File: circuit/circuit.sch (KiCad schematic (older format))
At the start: 9 parts

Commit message: Update schematic
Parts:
- gave numbers to parts that had none: 1
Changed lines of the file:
@@
 $EndDescr
-$Comp
-L Device:R_POT_US RV_THRESHOLD1
-U 1 1 61422150
-P 2950 1700
-F 0 "RV_THRESHOLD1" H 2882 1746 50  0000 R CNN
-F 1 "200K" H 2882 1655 50  0000 R CNN
-F 2 "" H 2950 1700 50  0001 C CNN
-F 3 "~" H 2950 1700 50  0001 C CNN
-	1    2950 1700
-	1    0    0    -1
-$EndComp
 $Comp
 L power:+5V #PWR0101
@@
 	1    0    0    -1
 $EndComp
-$Comp
-L power:Earth #PWR0102
-U 1 1 6142409F
-P 2950 1950
-F 0 "#PWR0102" H 2950 1700 50  0001 C CNN
-F 1 "Earth" H 2950 1800 50  0001 C CNN
-F 2 "" H 2950 1950 50  0001 C CNN
-F 3 "~" H 2950 1950 50  0001 C CNN
-	1    2950 1950
-	1    0    0    -1
-$EndComp
-Wire Wire Line
-	2950 1850 2950 1950
 Wire Wire Line
 	2950 1400 2950 1550
-Wire Wire Line
-	4550 1700 4550 2250
-Wire Wire Line
-	4550 2250 4450 2250
-Wire Wire Line
-	3700 2150 3850 2150
-Wire Wire Line
-	3650 2350 3750 2350
-Wire Wire Line
-	3050 2250 2800 2250
 Wire Wire Line
 	2800 2250 2800 2350
@@
 	1    0    0    -1
 $EndComp
-$Comp
-L Device:R_US R1
-U 1 1 6142A93A
-P 3250 2800
-F 0 "R1" V 3455 2800 50  0000 C CNN
-F 1 "150K" V 3364 2800 50  0000 C CNN
-F 2 "Resistor_THT:R_Axial_DIN0207_L6.3mm_D2.5mm_P10.16mm_Horizontal" V 3290 2790 50  0001 C CNN
-F 3 "~" H 3250 2800 50  0001 C CNN
-	1    3250 2800
-	0    -1   -1   0
-$EndComp
-Wire Wire Line
-	3400 2800 3750 2800
-Wire Wire Line
-	3750 2800 3750 2350
-Wire Wire Line
-	3100 2800 2950 2800
-Wire Wire Line
-	2950 2800 2950 2450
-Wire Wire Line
-	2950 2450 3050 2450
 $Comp
 L Device:D_Photo D1
@@
 $EndComp
 Wire Wire Line
-	2950 2800 2950 2900
-Connection ~ 2950 2800
-Wire Wire Line
 	2950 3200 2950 3300
 $Comp
@@
 	1    0    0    -1
 $EndComp
-Wire Wire Line
-	4650 2250 4550 2250
-Connection ~ 4550 2250
 Text GLabel 5250 2250 2    50   Output ~ 0
 IMPULSE_OUT
@@
 	5250 2250 4950 2250
 Connection ~ 4950 2250
-Wire Wire Line
-	3850 2350 3750 2350
-Connection ~ 3750 2350
-$Comp
-L Device:R_US R3
-U 1 1 61440E5A
-P 3900 1700
-F 0 "R3" V 4105 1700 50  0000 C CNN
-F 1 "18K" V 4014 1700 50  0000 C CNN
-F 2 "Resistor_THT:R_Axial_DIN0207_L6.3mm_D2.5mm_P10.16mm_Horizontal" V 3940 1690 50  0001 C CNN
-F 3 "~" H 3900 1700 50  0001 C CNN
-	1    3900 1700
-	0    -1   -1   0
-$EndComp
-Wire Wire Line
-	3700 1700 3700 2150
-$Comp
-L Device:R_US R2
-U 1 1 6144199F
-P 3500 1700
-F 0 "R2" V 3705 1700 50  0000 C CNN
-F 1 "1K" V 3614 1700 50  0000 C CNN
-F 2 "Resistor_THT:R_Axial_DIN0207_L6.3mm_D2.5mm_P10.16mm_Horizontal" V 3540 1690 50  0001 C CNN
-F 3 "~" H 3500 1700 50  0001 C CNN
-	1    3500 1700
-	0    -1   -1   0
-$EndComp
-Wire Wire Line
-	3650 1700 3700 1700
-Wire Wire Line
-	3700 1700 3750 1700
-Connection ~ 3700 1700
-Wire Wire Line
-	4050 1700 4550 1700
-Wire Wire Line
-	3350 1700 3100 1700
 Text Notes 3450 1400 0    50   ~ 0
 A ratio of 1/18 here gives 0.28 volts of hysteresis on the comparison.
-$Comp
-L dk_Linear-Amplifiers-Instrumentation-OP-Amps-Buffer-Amps:LM324AN U?
+Connection ~ 4150 2550
+Wire Wire Line
+	4150 2550 4400 2550
+$Comp
+L power:+5V #PWR0106
+U 1 1 61451173
+P 4400 2550
+F 0 "#PWR0106" H 4400 2400 50  0001 C CNN
+F 1 "+5V" H 4415 2723 50  0000 C CNN
+F 2 "" H 4400 2550 50  0001 C CNN
+F 3 "" H 4400 2550 50  0001 C CNN
+	1    4400 2550
+	1    0    0    -1
+$EndComp
+Connection ~ 3350 2050
+Wire Wire Line
+	3350 1950 3350 2050
+Wire Wire Line
+	4150 1950 3350 1950
+Wire Wire Line
+	4150 2050 4150 1950
+Wire Wire Line
+	4150 2550 4150 2450
+Wire Wire Line
+	3350 2550 4150 2550
+$Comp
+L dk_Linear-Amplifiers-Instrumentation-OP-Amps-Buffer-Amps:LM324AN U1
+U 2 1 6144BF1C
+P 4150 2250
+F 0 "U1" H 4150 1847 60  0000 C CNN
+F 1 "LM324AN" H 4150 1953 60  0000 C CNN
+F 2 "digikey-footprints:DIP-14_W3mm" H 4350 2450 60  0001 L CNN
+F 3 "http://www.ti.com/general/docs/suppproductinfo.tsp?distId=10&gotoUrl=http%3A%2F%2Fwww.ti.com%2Flit%2Fgpn%2Flm224" H 4350 2550 60  0001 L CNN
+F 4 "296-9542-5-ND" H 4350 2650 60  0001 L CNN "Digi-Key_PN"
+F 5 "LM324AN" H 4350 2750 60  0001 L CNN "MPN"
+F 6 "Integrated Circuits (ICs)" H 4350 2850 60  0001 L CNN "Category"
+F 7 "Linear - Amplifiers - Instrumentation, OP Amps, Buffer Amps" H 4350 2950 60  0001 L CNN "Family"
+F 8 "http://www.ti.com/general/docs/suppproductinfo.tsp?distId=10&gotoUrl=http%3A%2F%2Fwww.ti.com%2Flit%2Fgpn%2Flm224" H 4350 3050 60  0001 L CNN "DK_Datasheet_Link"
+F 9 "/product-detail/en/texas-instruments/LM324AN/296-9542-5-ND/412056" H 4350 3150 60  0001 L CNN "DK_Detail_Page"
+F 10 "IC OPAMP GP 4 CIRCUIT 14DIP" H 4350 3250 60  0001 L CNN "Description"
+F 11 "Texas Instruments" H 4350 3350 60  0001 L CNN "Manufacturer"
+F 12 "Active" H 4350 3450 60  0001 L CNN "Status"
+	2    4150 2250
+	1    0    0    1
+$EndComp
+Connection ~ 3050 2250
+Wire Wire Line
+	3050 2050 3050 2250
+Wire Wire Line
+	3350 2050 3050 2050
+Wire Wire Line
+	3350 2150 3350 2050
+$Comp
+L dk_Linear-Amplifiers-Instrumentation-OP-Amps-Buffer-Amps:LM324AN U1
 U 1 1 61447FCC
 P 3350 2350
-F 0 "U?" H 3350 1947 60  0000 C CNN
+F 0 "U1" H 3350 1947 60  0000 C CNN
 F 1 "LM324AN" H 3350 2053 60  0000 C CNN
 F 2 "digikey-footprints:DIP-14_W3mm" H 3550 2550 60  0001 L CNN
@@
 $EndComp
 Wire Wire Line
-	3350 2150 3350 2050
-Wire Wire Line
-	3350 2050 3050 2050
-Wire Wire Line
-	3050 2050 3050 2250
-Connection ~ 3050 2250
-$Comp
-L dk_Linear-Amplifiers-Instrumentation-OP-Amps-Buffer-Amps:LM324AN U?
-U 2 1 6144BF1C
-P 4150 2250
-F 0 "U?" H 4150 1847 60  0000 C CNN
-F 1 "LM324AN" H 4150 1953 60  0000 C CNN
-F 2 "digikey-footprints:DIP-14_W3mm" H 4350 2450 60  0001 L CNN
-F 3 "http://www.ti.com/general/docs/suppproductinfo.tsp?distId=10&gotoUrl=http%3A%2F%2Fwww.ti.com%2Flit%2Fgpn%2Flm224" H 4350 2550 60  0001 L CNN
-F 4 "296-9542-5-ND" H 4350 2650 60  0001 L CNN "Digi-Key_PN"
-F 5 "LM324AN" H 4350 2750 60  0001 L CNN "MPN"
-F 6 "Integrated Circuits (ICs)" H 4350 2850 60  0001 L CNN "Category"
-F 7 "Linear - Amplifiers - Instrumentation, OP Amps, Buffer Amps" H 4350 2950 60  0001 L CNN "Family"
-F 8 "http://www.ti.com/general/docs/suppproductinfo.tsp?distId=10&gotoUrl=http%3A%2F%2Fwww.ti.com%2Flit%2Fgpn%2Flm224" H 4350 3050 60  0001 L CNN "DK_Datasheet_Link"
-F 9 "/product-detail/en/texas-instruments/LM324AN/296-9542-5-ND/412056" H 4350 3150 60  0001 L CNN "DK_Detail_Page"
-F 10 "IC OPAMP GP 4 CIRCUIT 14DIP" H 4350 3250 60  0001 L CNN "Description"
-F 11 "Texas Instruments" H 4350 3350 60  0001 L CNN "Manufacturer"
-F 12 "Active" H 4350 3450 60  0001 L CNN "Status"
-	2    4150 2250
-	1    0    0    1
-$EndComp
-Wire Wire Line
-	3350 2550 4150 2550
-Wire Wire Line
-	4150 2550 4150 2450
-Wire Wire Line
-	4150 2050 4150 1950
-Wire Wire Line
-	4150 1950 3350 1950
-Wire Wire Line
-	3350 1950 3350 2050
-Connection ~ 3350 2050
-$Comp
-L power:+5V #PWR?
-U 1 1 61451173
-P 4400 2550
-F 0 "#PWR?" H 4400 2400 50  0001 C CNN
-F 1 "+5V" H 4415 2723 50  0000 C CNN
-F 2 "" H 4400 2550 50  0001 C CNN
-F 3 "" H 4400 2550 50  0001 C CNN
-	1    4400 2550
-	1    0    0    -1
-$EndComp
-Wire Wire Line
-	4150 2550 4400 2550
-Connection ~ 4150 2550
+	3350 1700 3100 1700
+Wire Wire Line
+	4050 1700 4550 1700
+Connection ~ 3700 1700
+Wire Wire Line
+	3700 1700 3750 1700
+Wire Wire Line
+	3650 1700 3700 1700
+$Comp
+L Device:R_US R2
+U 1 1 6144199F
+P 3500 1700
+F 0 "R2" V 3705 1700 50  0000 C CNN
+F 1 "1K" V 3614 1700 50  0000 C CNN
+F 2 "Resistor_THT:R_Axial_DIN0207_L6.3mm_D2.5mm_P10.16mm_Horizontal" V 3540 1690 50  0001 C CNN
+F 3 "~" H 3500 1700 50  0001 C CNN
+	1    3500 1700
+	0    -1   -1   0
+$EndComp
+Wire Wire Line
+	3700 1700 3700 2150
+$Comp
+L Device:R_US R3
+U 1 1 61440E5A
+P 3900 1700
+F 0 "R3" V 4105 1700 50  0000 C CNN
+F 1 "18K" V 4014 1700 50  0000 C CNN
+F 2 "Resistor_THT:R_Axial_DIN0207_L6.3mm_D2.5mm_P10.16mm_Horizontal" V 3940 1690 50  0001 C CNN
+F 3 "~" H 3900 1700 50  0001 C CNN
+	1    3900 1700
+	0    -1   -1   0
+$EndComp
+Connection ~ 3750 2350
+Wire Wire Line
+	3850 2350 3750 2350
+Connection ~ 4550 2250
+Wire Wire Line
+	4650 2250 4550 2250
+Connection ~ 2950 2800
+Wire Wire Line
+	2950 2800 2950 2900
+Wire Wire Line
+	2950 2450 3050 2450
+Wire Wire Line
+	2950 2800 2950 2450
+Wire Wire Line
+	3100 2800 2950 2800
+Wire Wire Line
+	3750 2800 3750 2350
+Wire Wire Line
+	3400 2800 3750 2800
+$Comp
+L Device:R_US R1
+U 1 1 6142A93A
+P 3250 2800
+F 0 "R1" V 3455 2800 50  0000 C CNN
+F 1 "150K" V 3364 2800 50  0000 C CNN
+F 2 "Resistor_THT:R_Axial_DIN0207_L6.3mm_D2.5mm_P10.16mm_Horizontal" V 3290 2790 50  0001 C CNN
+F 3 "~" H 3250 2800 50  0001 C CNN
+	1    3250 2800
+	0    -1   -1   0
+$EndComp
+Wire Wire Line
+	3050 2250 2800 2250
+Wire Wire Line
+	3650 2350 3750 2350
+Wire Wire Line
+	3700 2150 3850 2150
+Wire Wire Line
+	4550 2250 4450 2250
+Wire Wire Line
+	4550 1700 4550 2250
+Wire Wire Line
+	2950 1850 2950 1950
+$Comp
+L power:Earth #PWR0102
+U 1 1 6142409F
+P 2950 1950
+F 0 "#PWR0102" H 2950 1700 50  0001 C CNN
+F 1 "Earth" H 2950 1800 50  0001 C CNN
+F 2 "" H 2950 1950 50  0001 C CNN
+F 3 "~" H 2950 1950 50  0001 C CNN
+	1    2950 1950
+	1    0    0    -1
+$EndComp
+$Comp
+L Device:R_POT_US RV_THRESHOLD1
+U 1 1 61422150
+P 2950 1700
+F 0 "RV_THRESHOLD1" H 2882 1746 50  0000 R CNN
+F 1 "200K" H 2882 1655 50  0000 R CNN
+F 2 "" H 2950 1700 50  0001 C CNN
+F 3 "~" H 2950 1700 50  0001 C CNN
+	1    2950 1700
+	1    0    0    -1
+$EndComp
 $EndSCHEMATC

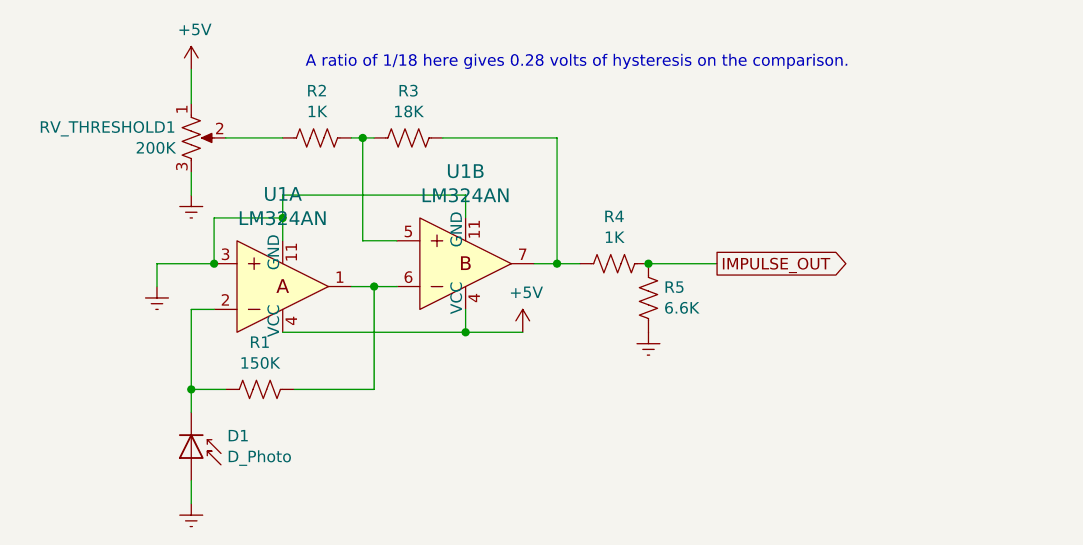
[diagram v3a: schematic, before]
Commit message: Increase amplification for photodiode
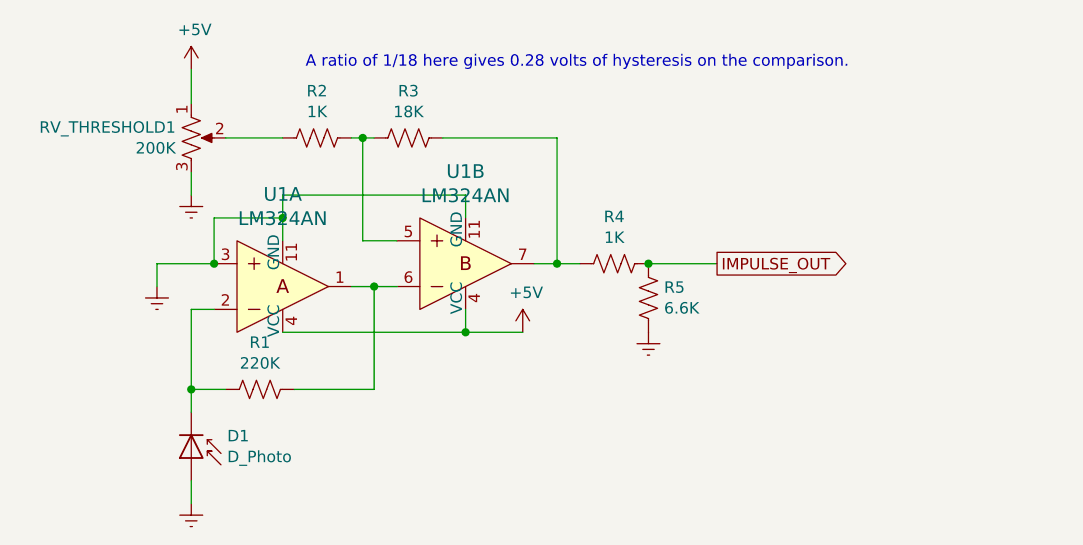
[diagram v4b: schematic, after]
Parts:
- R1: value 150K -> 220K
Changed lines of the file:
@@
 P 3250 2800
 F 0 "R1" V 3455 2800 50  0000 C CNN
-F 1 "150K" V 3364 2800 50  0000 C CNN
+F 1 "220K" V 3364 2800 50  0000 C CNN
 F 2 "Resistor_THT:R_Axial_DIN0207_L6.3mm_D2.5mm_P10.16mm_Horizontal" V 3290 2790 50  0001 C CNN
 F 3 "~" H 3250 2800 50  0001 C CNN
